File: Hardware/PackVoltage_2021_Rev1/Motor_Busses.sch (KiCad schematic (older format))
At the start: 50 parts, among them Q1 Q_NMOS_DGS, Q2 Q_NMOS_DGS, Q3 Q_NMOS_DGS, Q4 Q_NMOS_DGS, Q9 Q_NMOS_DGS, U10 LT1910, U11 INA281, U2 LT1910, U3 LT1910, U4 LT1910, U5 INA281, U6 INA281, U7 INA281, U8 LT1910, U9 INA281

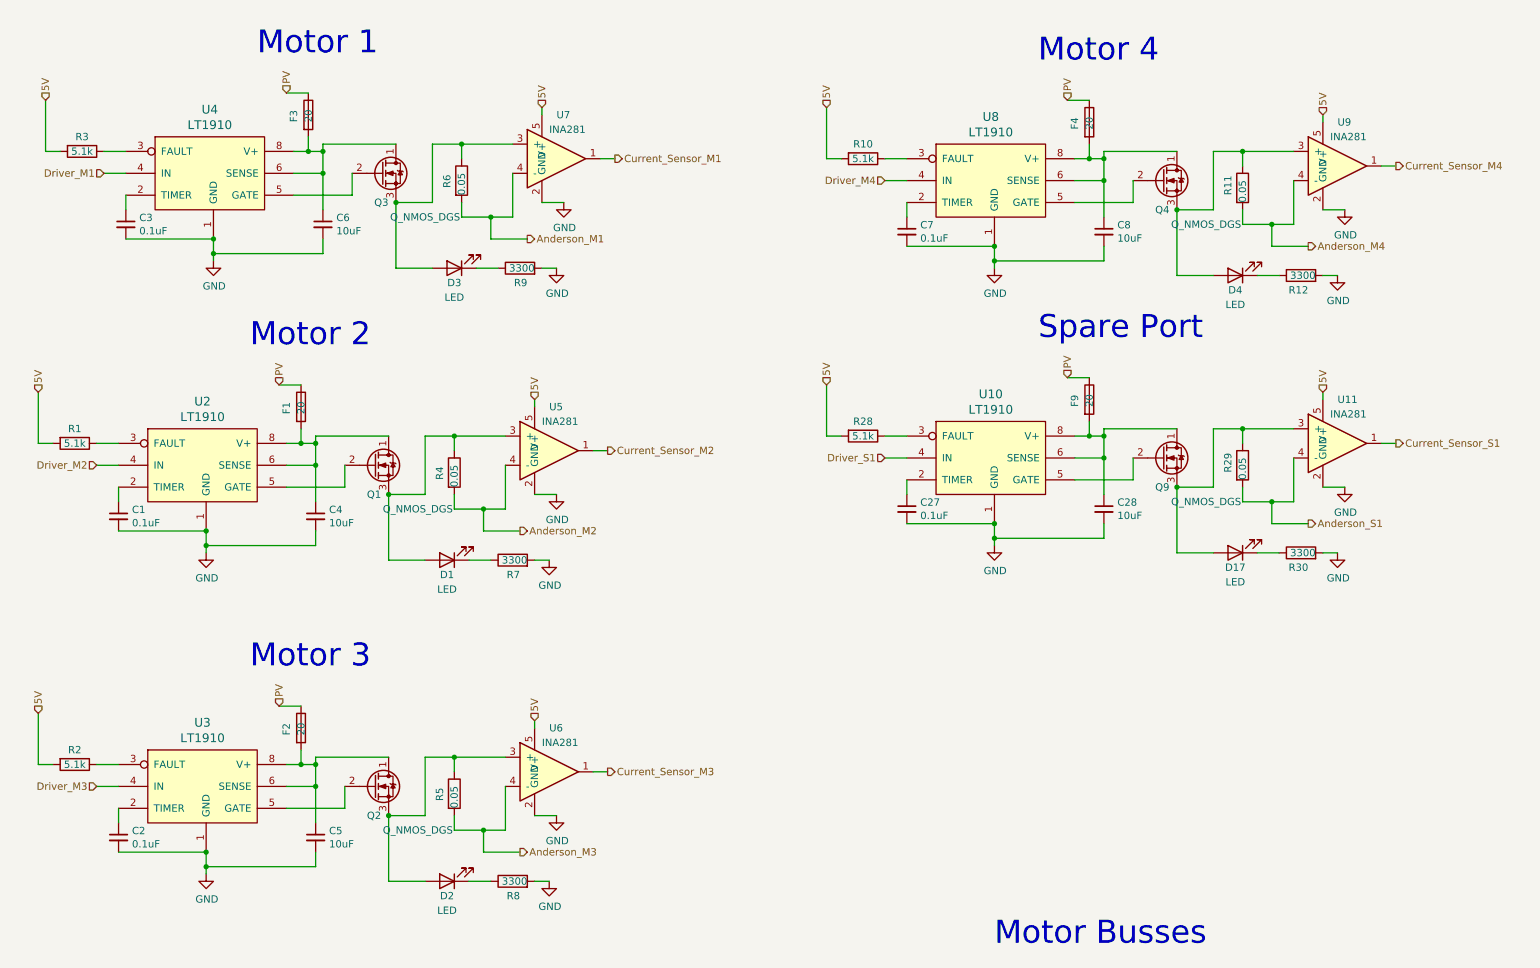
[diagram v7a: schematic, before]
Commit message: Added GimbalSense, reannotated
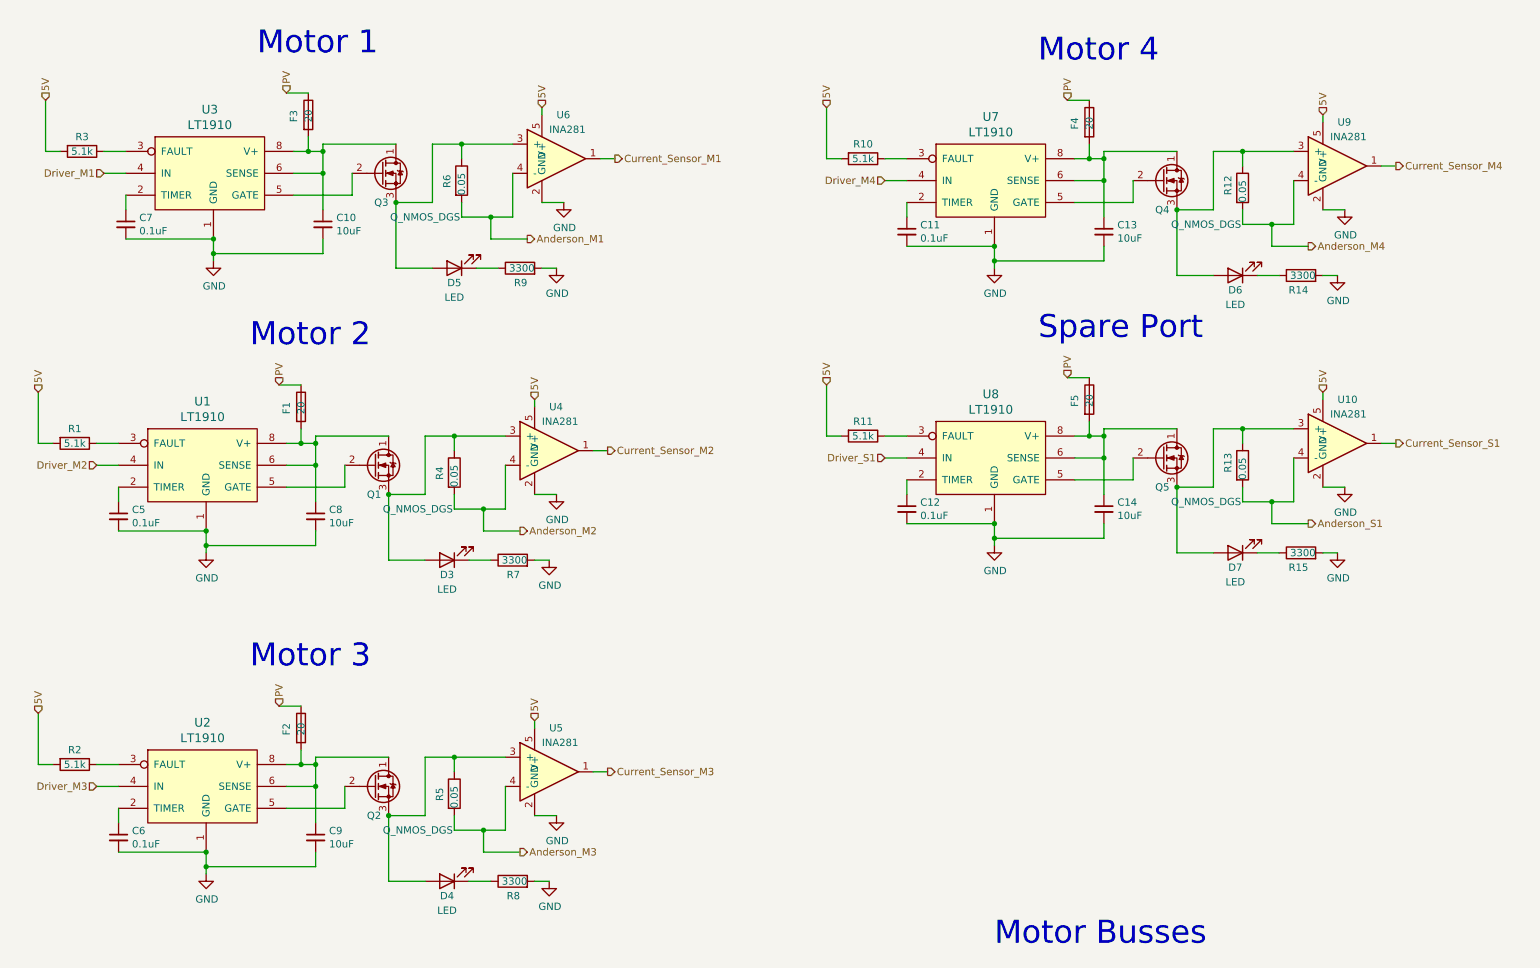
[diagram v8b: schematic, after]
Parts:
- renumbered C6 to C10, C7 to C11, C27 to C12, C8 to C13, C28 to C14, C1 to C5, C2 to C6, C3 to C7, C4 to C8, C5 to C9, D1 to D3, D2 to D4, D3 to D5, D4 to D6, D17 to D7, F9 to F5, Q9 to Q5, R28 to R11, R11 to R12, R29 to R13, R12 to R14, R30 to R15, U2 to U1, U11 to U10, U3 to U2, U4 to U3, U5 to U4, U6 to U5, U7 to U6, U8 to U7, U10 to U8
